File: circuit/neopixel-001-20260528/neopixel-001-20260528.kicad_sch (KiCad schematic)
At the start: 47 parts, among them SW1 SW_SPST, SW2 SW_SPST, SW3 SW_SPST, SW4 SW_SPST

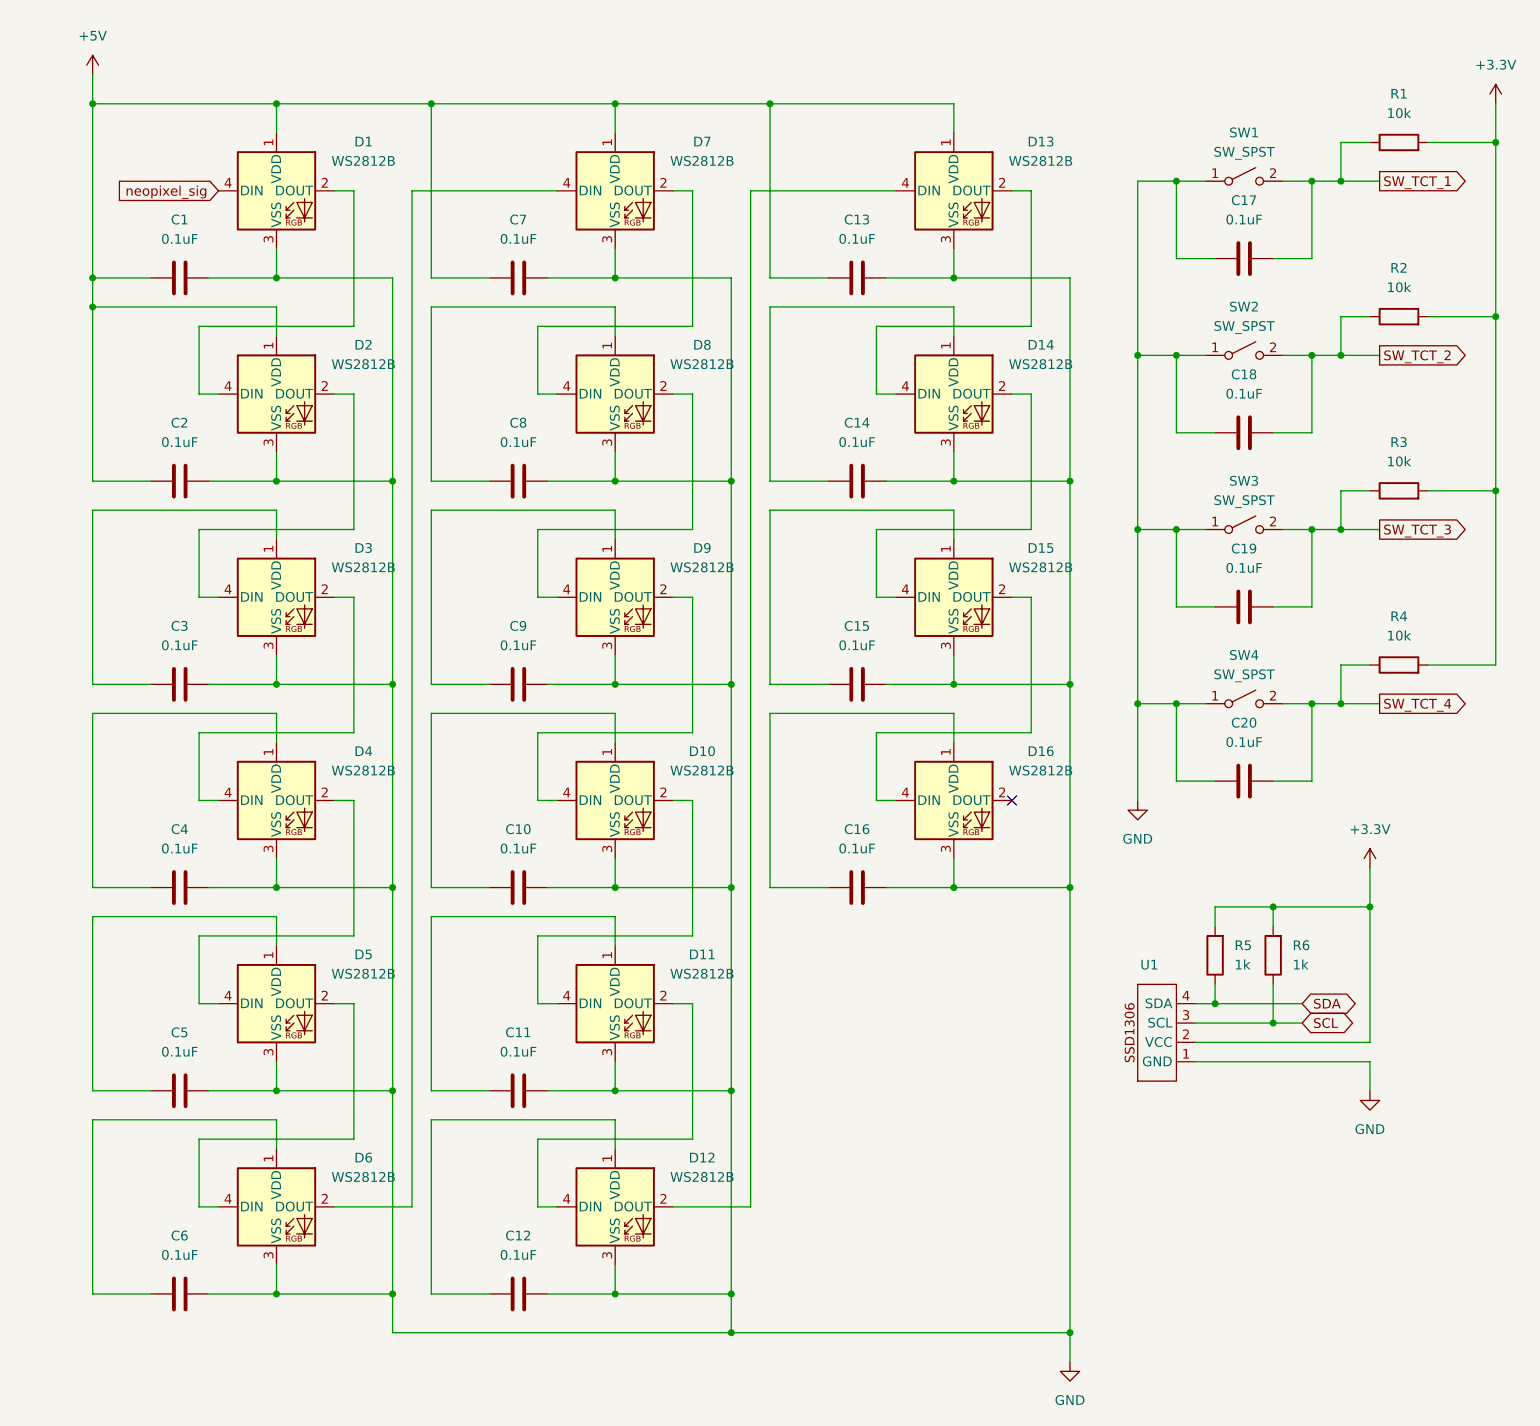
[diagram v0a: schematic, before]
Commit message: Update NeoPixel基板の回路図を仮完成させた
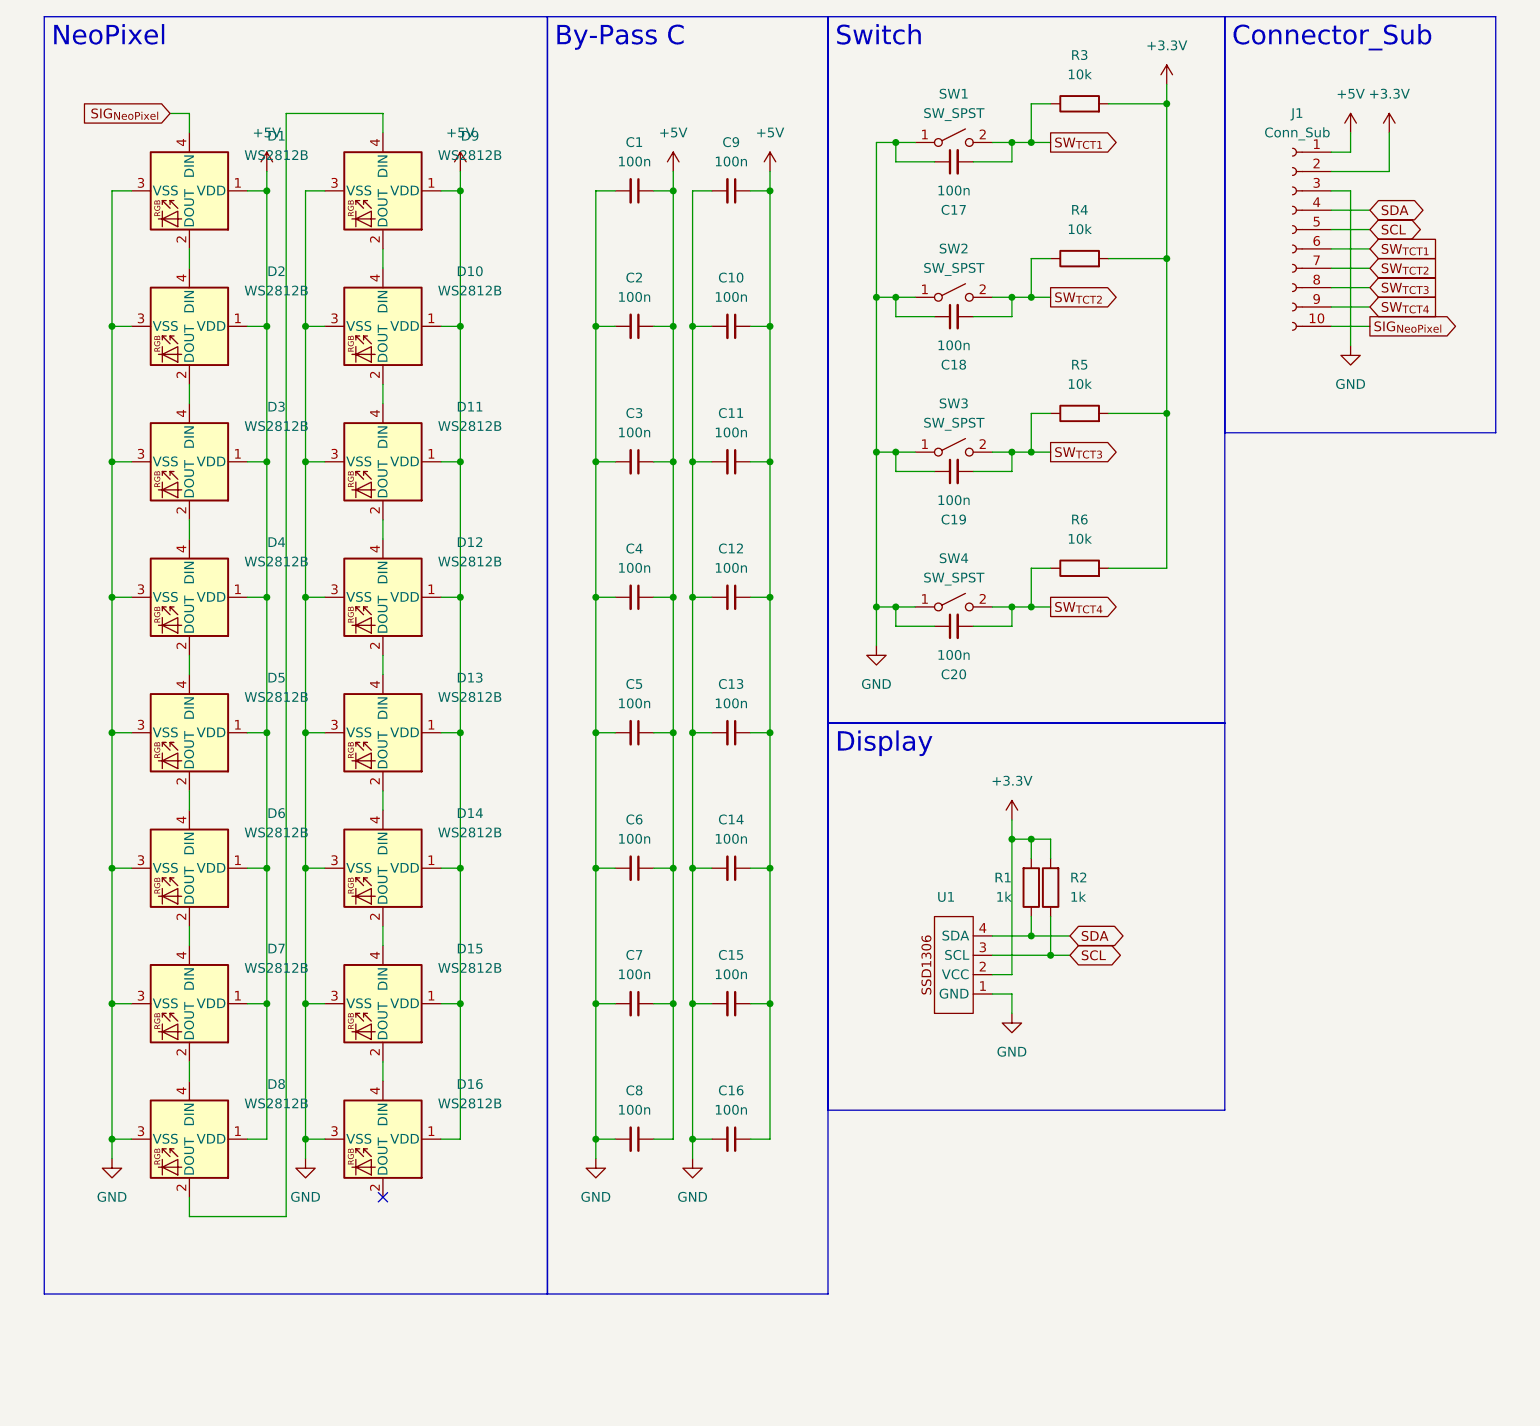
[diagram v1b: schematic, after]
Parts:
- removed C1, C10, C11, C12, C13, C14, C15, C16, C17, C18, C19, C2, C20, C3, C4, C5, C6, C7, C8, C9: 0.1uF, symbol Device:C
- removed R1, R2: 10k, symbol Device:R
- added C1, C10, C11, C12, C13, C14, C15, C16, C17, C18, C19, C2, C20, C3, C4, C5, C6, C7, C8, C9: 100n, symbol Device:C_Small
- added J1: Conn_Sub, symbol Connector:Conn_01x10_Socket
- added R4, R5: 10k, symbol Device:R
- renumbered R5 to R1, R6 to R2, R4 to R6
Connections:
- net +3.3V: now also J1.2 (Pin_2), R4.2, R5.2
- net +5V: now also D10.1 (VDD), D11.1 (VDD), D12.1 (VDD), D14.1 (VDD), D15.1 (VDD), D16.1 (VDD), D3.1 (VDD), D4.1 (VDD), D5.1 (VDD), D6.1 (VDD), D8.1 (VDD), D9.1 (VDD), C1.1, C10.1, C11.1, C12.1, C13.1, C14.1, C15.1, C16.1, C2.1, C3.1, C4.1, C5.1, C6.1, C7.1, C8.1, C9.1, J1.1 (Pin_1)
- net GND: now also C1.2, C10.2, C11.2, C12.2, C13.2, C14.2, C15.2, C16.2, C17.1, C18.1, C19.1, C2.2, C20.1, C3.2, C4.2, C5.2, C6.2, C7.2, C8.2, C9.2, J1.3 (Pin_3)
- net SCL: now also J1.5 (Pin_5)
- net SDA: now also J1.4 (Pin_4)
- net SW_TCT_1 renamed SW_{TCT1}
- net SW_{TCT1}: now also R3.1, C17.2, J1.6 (Pin_6)
- net SW_TCT_2 renamed SW_{TCT2}
- net SW_{TCT2}: now also C18.2, J1.7 (Pin_7), R4.1
- net SW_TCT_3 renamed SW_{TCT3}
- net SW_{TCT3}: now also C19.2, J1.8 (Pin_8), R5.1; no longer R3.1
- net SW_TCT_4 renamed SW_{TCT4}
- net SW_{TCT4}: now also C20.2, J1.9 (Pin_9)
- net neopixel_sig renamed SIG_{NeoPixel}
- net SIG_{NeoPixel}: now also J1.10 (Pin_10)
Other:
- moved on the sheet: R1, R2, R6, SW4, U1

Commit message: Update 供給基板のボード図の修正とDR完了、再DR求
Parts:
- added P1: USB_C_Plug, symbol Connector:USB_C_Plug
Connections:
- net GND: now also P1.A1 (GND), P1.A12 (GND), P1.B1 (GND), P1.B12 (GND)
- new net: P1.A4 (VBUS), P1.A9 (VBUS), P1.B4 (VBUS), P1.B9 (VBUS)
- no-connect marks 1 -> 2
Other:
- moved on the sheet: J1, R1, R2, U1

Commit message: Update NeoPixel基板の回路図が完成
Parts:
- removed J1: Conn_Sub, symbol Connector:Conn_01x10_Socket
- removed U1: (no value), symbol @Thrive_symbol_neopixel:SSD1306
- added J1: Conn_NeoPixel, Connector_FFC-FPC:JUSHUO_AFA07-S12FCA-00_1x12-1MP_P1.0mm_Horizontal, symbol Connector:Conn_01x12_Socket
- added P10: unitV3, symbol Connector:USB_C_Plug
- added P11: unitV4, Connector_USB:USB_C_Receptacle_GCT_USB4105-xx-A_16P_TopMnt_Horizontal, symbol Connector:USB_C_Plug
- added P12: unitV4, symbol Connector:USB_C_Plug
- added P2: ESP32C3_{1}, symbol Connector:USB_C_Plug
- added P3: ESP32C3_{2}, Connector_USB:USB_C_Receptacle_GCT_USB4105-xx-A_16P_TopMnt_Horizontal, symbol Connector:USB_C_Plug
- added P4: ESP32C3_{2}, symbol Connector:USB_C_Plug
- added P5: unitV1, Connector_USB:USB_C_Receptacle_GCT_USB4105-xx-A_16P_TopMnt_Horizontal, symbol Connector:USB_C_Plug
- added P6: unitV1, symbol Connector:USB_C_Plug
- added P7: unitV2, Connector_USB:USB_C_Receptacle_GCT_USB4105-xx-A_16P_TopMnt_Horizontal, symbol Connector:USB_C_Plug
- added P8: unitV2, symbol Connector:USB_C_Plug
- added P9: unitV3, Connector_USB:USB_C_Receptacle_GCT_USB4105-xx-A_16P_TopMnt_Horizontal, symbol Connector:USB_C_Plug
- added U1: SSD1306, @Thrive_footprint_neopixel:SSD1306_display_module, symbol @Thrive_symbol_neopixel:SSD1306_display_module
- C1, C10, C11, C12, C13, C14, C15, C16, C17, C18, C19, C2, C20, C3, C4, C5, C6, C7, C8, C9: footprint (none) -> Capacitor_SMD:C_0805_2012Metric
- P1: value USB_C_Plug -> ESP32C3_{1}; footprint (none) -> Connector_USB:USB_C_Receptacle_GCT_USB4105-xx-A_16P_TopMnt_Horizontal
- R1, R2, R3, R4, R5, R6: footprint (none) -> Resistor_SMD:R_0805_2012Metric
- SW1, SW2, SW3, SW4: footprint (none) -> @Thrive_footprint_neopixel:ST-12-401FC-G
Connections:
- net +3.3V: now also J1.3 (Pin_3), U1.2 (VCC)
- net +5V: now also J1.1 (Pin_1), J1.2 (Pin_2)
- net GND: now also J1.4 (Pin_4), J1.5 (Pin_5), P10.A1 (GND), P10.A12 (GND), P10.B1 (GND), P10.B12 (GND), P11.A1 (GND), P11.A12 (GND), P11.B1 (GND), P11.B12 (GND), P12.A1 (GND), P12.A12 (GND), P12.B1 (GND), P12.B12 (GND), P2.A1 (GND), P2.A12 (GND), P2.B1 (GND), P2.B12 (GND), P3.A1 (GND), P3.A12 (GND), P3.B1 (GND), P3.B12 (GND), P4.A1 (GND), P4.A12 (GND), P4.B1 (GND), P4.B12 (GND), P5.A1 (GND), P5.A12 (GND), P5.B1 (GND), P5.B12 (GND), P6.A1 (GND), P6.A12 (GND), P6.B1 (GND), P6.B12 (GND), P7.A1 (GND), P7.A12 (GND), P7.B1 (GND), P7.B12 (GND), P8.A1 (GND), P8.A12 (GND), P8.B1 (GND), P8.B12 (GND), P9.A1 (GND), P9.A12 (GND), P9.B1 (GND), P9.B12 (GND), U1.1 (GND)
- net SCL: now also J1.7 (Pin_7), U1.3 (SCL)
- net SDA: now also J1.6 (Pin_6), U1.4 (SDA)
- net SIG_{NeoPixel}: now also J1.12 (Pin_12)
- net SW_{TCT1}: now also J1.8 (Pin_8)
- net SW_{TCT2}: now also J1.9 (Pin_9)
- net SW_{TCT3}: now also J1.10 (Pin_10)
- net SW_{TCT4}: now also J1.11 (Pin_11)
- net at P1.A10 (RX2-): now also P2.A10 (RX2-)
- net at P1.A11 (RX2+): now also P2.A11 (RX2+)
- net at P1.A2 (TX1+): now also P2.A2 (TX1+)
- net at P1.A3 (TX1-): now also P2.A3 (TX1-)
- net at P1.A4 (VBUS), P1.A9 (VBUS), P1.B4 (VBUS)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: now also P2.A4 (VBUS), P2.A9 (VBUS), P2.B4 (VBUS), P2.B9 (VBUS)
- net at P1.A5 (CC): now also P2.A5 (CC)
- net at P1.A6 (D+): now also P2.A6 (D+)
- net at P1.A7 (D-): now also P2.A7 (D-)
- net at P1.A8 (SBU1): now also P2.A8 (SBU1)
- net at P1.B10 (RX1-): now also P2.B10 (RX1-)
- net at P1.B11 (RX1+): now also P2.B11 (RX1+)
- net at P1.B2 (TX2+): now also P2.B2 (TX2+)
- net at P1.B3 (TX2-): now also P2.B3 (TX2-)
- net at P1.B5 (VCONN): now also P2.B5 (VCONN)
- net at P1.B8 (SBU2): now also P2.B8 (SBU2)
- new net: P7.A10 (RX2-), P8.A10 (RX2-)
- new net: P7.A11 (RX2+), P8.A11 (RX2+)
- new net: P7.A2 (TX1+), P8.A2 (TX1+)
- new net: P7.A3 (TX1-), P8.A3 (TX1-)
- new net: P7.A4 (VBUS), P7.A9 (VBUS), P7.B4 (VBUS), P7.B9 (VBUS), P8.A4 (VBUS), P8.A9 (VBUS), P8.B4 (VBUS), P8.B9 (VBUS)
- new net: P7.A5 (CC), P8.A5 (CC)
- new net: P7.A6 (D+), P8.A6 (D+)
- new net: P7.A7 (D-), P8.A7 (D-)
- new net: P7.A8 (SBU1), P8.A8 (SBU1)
- new net: P7.B10 (RX1-), P8.B10 (RX1-)
- new net: P7.B11 (RX1+), P8.B11 (RX1+)
- new net: P7.B2 (TX2+), P8.B2 (TX2+)
- new net: P7.B3 (TX2-), P8.B3 (TX2-)
- new net: P7.B5 (VCONN), P8.B5 (VCONN)
- new net: P7.B8 (SBU2), P8.B8 (SBU2)
- new net: P11.A10 (RX2-), P12.A10 (RX2-)
- new net: P11.A11 (RX2+), P12.A11 (RX2+)
- new net: P11.A2 (TX1+), P12.A2 (TX1+)
- new net: P11.A3 (TX1-), P12.A3 (TX1-)
- new net: P11.A4 (VBUS), P11.A9 (VBUS), P11.B4 (VBUS), P11.B9 (VBUS), P12.A4 (VBUS), P12.A9 (VBUS), P12.B4 (VBUS), P12.B9 (VBUS)
- new net: P11.A5 (CC), P12.A5 (CC)
- new net: P11.A6 (D+), P12.A6 (D+)
- new net: P11.A7 (D-), P12.A7 (D-)
- new net: P11.A8 (SBU1), P12.A8 (SBU1)
- new net: P11.B10 (RX1-), P12.B10 (RX1-)
- new net: P11.B11 (RX1+), P12.B11 (RX1+)
- new net: P11.B2 (TX2+), P12.B2 (TX2+)
- new net: P11.B3 (TX2-), P12.B3 (TX2-)
- new net: P11.B5 (VCONN), P12.B5 (VCONN)
- new net: P11.B8 (SBU2), P12.B8 (SBU2)
- new net: P5.A10 (RX2-), P6.A10 (RX2-)
- new net: P5.A11 (RX2+), P6.A11 (RX2+)
- new net: P5.A2 (TX1+), P6.A2 (TX1+)
- new net: P5.A3 (TX1-), P6.A3 (TX1-)
- new net: P5.A4 (VBUS), P5.A9 (VBUS), P5.B4 (VBUS), P5.B9 (VBUS), P6.A4 (VBUS), P6.A9 (VBUS), P6.B4 (VBUS), P6.B9 (VBUS)
- new net: P5.A5 (CC), P6.A5 (CC)
- new net: P5.A6 (D+), P6.A6 (D+)
- new net: P5.A7 (D-), P6.A7 (D-)
- new net: P5.A8 (SBU1), P6.A8 (SBU1)
- new net: P5.B10 (RX1-), P6.B10 (RX1-)
- new net: P5.B11 (RX1+), P6.B11 (RX1+)
- new net: P5.B2 (TX2+), P6.B2 (TX2+)
- new net: P5.B3 (TX2-), P6.B3 (TX2-)
- new net: P5.B5 (VCONN), P6.B5 (VCONN)
- new net: P5.B8 (SBU2), P6.B8 (SBU2)
- new net: P3.A10 (RX2-), P4.A10 (RX2-)
- new net: P3.A11 (RX2+), P4.A11 (RX2+)
- new net: P3.A2 (TX1+), P4.A2 (TX1+)
- new net: P3.A3 (TX1-), P4.A3 (TX1-)
- new net: P3.A4 (VBUS), P3.A9 (VBUS), P3.B4 (VBUS), P3.B9 (VBUS), P4.A4 (VBUS), P4.A9 (VBUS), P4.B4 (VBUS), P4.B9 (VBUS)
- new net: P3.A5 (CC), P4.A5 (CC)
- new net: P3.A6 (D+), P4.A6 (D+)
- new net: P3.A7 (D-), P4.A7 (D-)
- new net: P3.A8 (SBU1), P4.A8 (SBU1)
- new net: P3.B10 (RX1-), P4.B10 (RX1-)
- new net: P3.B11 (RX1+), P4.B11 (RX1+)
- new net: P3.B2 (TX2+), P4.B2 (TX2+)
- new net: P3.B3 (TX2-), P4.B3 (TX2-)
- new net: P3.B5 (VCONN), P4.B5 (VCONN)
- new net: P3.B8 (SBU2), P4.B8 (SBU2)
- new net: P10.A10 (RX2-), P9.A10 (RX2-)
- new net: P10.A11 (RX2+), P9.A11 (RX2+)
- new net: P10.A2 (TX1+), P9.A2 (TX1+)
- new net: P10.A3 (TX1-), P9.A3 (TX1-)
- new net: P10.A4 (VBUS), P10.A9 (VBUS), P10.B4 (VBUS), P10.B9 (VBUS), P9.A4 (VBUS), P9.A9 (VBUS), P9.B4 (VBUS), P9.B9 (VBUS)
- new net: P10.A5 (CC), P9.A5 (CC)
- new net: P10.A6 (D+), P9.A6 (D+)
- new net: P10.A7 (D-), P9.A7 (D-)
- new net: P10.A8 (SBU1), P9.A8 (SBU1)
- new net: P10.B10 (RX1-), P9.B10 (RX1-)
- new net: P10.B11 (RX1+), P9.B11 (RX1+)
- new net: P10.B2 (TX2+), P9.B2 (TX2+)
- new net: P10.B3 (TX2-), P9.B3 (TX2-)
- new net: P10.B5 (VCONN), P9.B5 (VCONN)
- new net: P10.B8 (SBU2), P9.B8 (SBU2)
- no-connect marks 2 -> 13
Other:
- moved on the sheet: P1
